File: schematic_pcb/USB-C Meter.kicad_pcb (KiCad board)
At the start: 2 copper layers, 58.5 x 48 mm, 11 parts, among them J1 USB_C_Receptacle_PowerOnly_6P, J2 USB_C_Receptacle_PowerOnly_6P, U1 WEMOS_D1_mini, U2 INA226, U3 Display I2C

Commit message: feat: pcb/schematic v2.1.0
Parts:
- removed R5: 3k3, Resistor_SMD:R_0402_1005Metric
- added C1: 33µF/35V, Capacitor_SMD:CP_Elec_5x5.8, F.Cu at (71.5, 33.0)
- added C10: 0.1µ, Capacitor_SMD:C_0603_1608Metric, B.Cu at (87.5, 53.5)
- added C11: 1µ, Capacitor_SMD:C_0603_1608Metric, B.Cu at (78.0, 51.5)
- added C12: 0.1µ, Capacitor_SMD:C_0603_1608Metric, B.Cu at (78.0, 50.0)
- added C14: 1µ, Capacitor_SMD:C_0603_1608Metric, B.Cu at (84.3, 42.0)
- added C15: 10n, Capacitor_SMD:C_0603_1608Metric, B.Cu at (85.8, 42.0)
- added C16: 0.1µ, Capacitor_SMD:C_0603_1608Metric, B.Cu at (89.5, 49.5)
- added C17: 1pF, Capacitor_SMD:C_0402_1005Metric, B.Cu at (88.0, 43.0)
- added C18: 1pF, Capacitor_SMD:C_0402_1005Metric, B.Cu at (88.0, 41.0)
- added C20: 0.1µ, Capacitor_SMD:C_0603_1608Metric, B.Cu at (85.8, 60.2)
- added C21: 0.1µ, Capacitor_SMD:C_0603_1608Metric, B.Cu at (82.8, 60.2)
- added C3: 10µF, Capacitor_SMD:C_0603_1608Metric, B.Cu at (73.1, 35.2)
- added C5: 10pF, Capacitor_SMD:C_0402_1005Metric, B.Cu at (81.8, 41.0)
- added C6: 220µF, Capacitor_SMD:CP_Elec_6.3x5.9, F.Cu at (94.0, 33.0)
- added C7: 220µF, Capacitor_SMD:CP_Elec_6.3x5.9, F.Cu at (82.5, 33.0)
- added C8: 0.1µ, Capacitor_SMD:C_0603_1608Metric, B.Cu at (77.0, 32.5)
- added C9: 10µF, Capacitor_SMD:C_0603_1608Metric, B.Cu at (78.5, 32.5)
- added D1: 1N5819WS, Diode_SMD:D_SOD-323, B.Cu at (67.0, 33.0)
- added D2: PMEG2005EH, Diode_SMD:D_SOD-123F, B.Cu at (100.0, 33.0)
- added D3: 1N5819WS, Diode_SMD:D_SOD-323, B.Cu at (70.0, 42.0)
- added D4: 1N5819WS, Diode_SMD:D_SOD-323, B.Cu at (96.5, 38.0)
- added J1: USB_B_Micro, Connector_USB:USB_Micro-B_Wuerth_629105150521, F.Cu at (62.4, 37.0)
- added J3: Generic IN, Connector_PinHeader_2.54mm:PinHeader_2x05_P2.54mm_Horizontal, F.Cu at (71.0, 56.2)
- added J4: Generic OUT, Connector_PinSocket_2.54mm:PinSocket_2x05_P2.54mm_Horizontal, F.Cu at (95.4, 56.3)
- added J6: Conn_Coaxial, Connector_Coaxial:U.FL_Hirose_U.FL-R-SMT-1_Vertical, F.Cu at (94.5, 41.0)
- added L1: 47µH, Inductor_SMD:L_Changjiang_FXL0630, F.Cu at (102.6, 36.8)
- added L2: 2.7nH, Inductor_SMD:L_0603_1608Metric_Pad1.05x0.95mm_HandSolder, B.Cu at (90.5, 42.0)
- added R10: 0.01R 3W, Resistor_SMD:R_2512_6332Metric, F.Cu at (83.5, 63.5)
- added R11: 10R, Resistor_SMD:R_0402_1005Metric, B.Cu at (85.5, 62.0)
- added R12: 12k, Resistor_SMD:R_0603_1608Metric_Pad0.98x0.95mm_HandSolder, B.Cu at (89.5, 51.0)
- added R2: 3k3, Resistor_SMD:R_0402_1005Metric, B.Cu at (87.5, 55.0)
- added R3: 400R, Resistor_SMD:R_0402_1005Metric, B.Cu at (84.0, 34.5)
- added R9: 10R, Resistor_SMD:R_0402_1005Metric, B.Cu at (83.0, 62.0)
- added REF**: MountingHole_2.2mm_M2_DIN965, MountingHole:MountingHole_2.2mm_M2_DIN965, F.Cu at (95.5, 62.2)
- added REF**: MountingHole_2.2mm_M2_DIN965, MountingHole:MountingHole_2.2mm_M2_DIN965, F.Cu at (62.0, 29.0)
- added REF**: MountingHole_2.2mm_M2_DIN965, MountingHole:MountingHole_2.2mm_M2_DIN965, F.Cu at (71.0, 62.2)
- added REF**: MountingHole_2.2mm_M2_DIN965, MountingHole:MountingHole_2.2mm_M2_DIN965, F.Cu at (104.5, 29.0)
- added U2: ME6211C33M5, Package_TO_SOT_SMD:SOT-23-5, B.Cu at (71.0, 32.5)
- added U3: TPS2115, Package_SO:TSSOP-8_4.4x3mm_P0.65mm, B.Cu at (84.0, 32.0)
- added U4: ESP32-C3FH4, Package_DFN_QFN:QFN-32-1EP_5x5mm_P0.5mm_EP3.7x3.7mm, B.Cu at (84.0, 48.0)
- added Y1: 40MHz, Crystal:Crystal_SMD_3225-4Pin_3.2x2.5mm, B.Cu at (79.0, 42.0)
- C13: renamed from C3; moved to B.Cu
- C2: value 20µ -> 10µF; footprint Capacitor_Tantalum_SMD:CP_EIA-6032-20_AVX-F -> Capacitor_SMD:C_0603_1608Metric; moved to B.Cu
- C4: value 0.1µ -> 10pF; footprint Capacitor_SMD:C_0603_1608Metric -> Capacitor_SMD:C_0402_1005Metric; moved to B.Cu
- J2: renamed from J1; value USB_C_Receptacle_PowerOnly_6P -> USB-C Receptacle 6P; footprint Connector_USB:USB_C_Receptacle_HRO_TYPE-C-31-M-17 -> Connector_USB:USB_C_Receptacle_GCT_USB4125-xx-x_6P_TopMnt_Horizontal
- J5: renamed from J2; value USB_C_Receptacle_PowerOnly_6P -> USB-C Receptacle 6P
- R1: value 0.01R 3W -> 3k3; footprint Resistor_SMD:R_1206_3216Metric -> Resistor_SMD:R_0402_1005Metric; moved to B.Cu
- R4: value 3k3 -> 12k; footprint Resistor_SMD:R_0402_1005Metric -> Resistor_SMD:R_0603_1608Metric_Pad0.98x0.95mm_HandSolder; moved to B.Cu
- U1: value WEMOS_D1_mini -> XL1509-3.3; footprint RF_Module:WEMOS_D1_mini_light -> Package_SO:SOIC-8_3.9x4.9mm_P1.27mm
- U6: renamed from U2; value INA226 -> INA228; moved to B.Cu
- U7: renamed from U3; footprint Connector_PinHeader_2.54mm:PinHeader_1x04_P2.54mm_Vertical -> Connector_PinSocket_2.54mm:PinSocket_1x04_P2.54mm_Vertical
- moved U1 27.6 mm to (94.0, 33.0), turned to 180 degrees
- moved C2 18.5 mm to (69.6, 35.2), turned to 180 degrees
- moved C4 14.4 mm to (81.8, 43.0), turned to 180 degrees
- moved J5 9.28 mm to (104.4, 64.0)
- moved R1 8.00 mm to (87.5, 56.5)
- moved C13 6.67 mm to (78.0, 48.5)
- moved U7 6.38 mm to (79.5, 38.5)
- moved U6 4.12 mm to (84.0, 56.0), turned to -90 degrees
- moved J2 3.54 mm to (62.0, 64.0)
- moved R4 2.50 mm to (89.5, 48.0), turned to 0 degrees
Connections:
- net Net-(J1-CC1) renamed /CC1
- net Net-(J1-CC2) renamed /CC2
- C13 pad 1: Net-(U1-3V3) -> GND
- C13 pad 2: Net-(J1-SHIELD) -> Net-(U4-VDD_SPI)
- C2 pad 1: Net-(U1-3V3) -> /VBUS_DATA_R
- C2 pad 2: Net-(J1-SHIELD) -> GND
- C4 pad 1: Net-(J1-SHIELD) -> Net-(U4-XTAL_N)
- C4 pad 2: Net-(U1-3V3) -> GND
- J2 pad A12: Net-(J1-SHIELD) -> GND
- J2 pad A9: Net-(U2-Vin+) -> /VBUS_PD_1_IN
- J2 pad B12: Net-(J1-SHIELD) -> GND
- J2 pad B9: Net-(U2-Vin+) -> /VBUS_PD_1_IN
- J2 pad S1: Net-(J1-SHIELD) -> GND
- J5 pad A12: Net-(J1-SHIELD) -> GND
- J5 pad A9: Net-(U2-Vbus) -> /VBUS_PD_2_IN
- J5 pad B12: Net-(J1-SHIELD) -> GND
- J5 pad B9: Net-(U2-Vbus) -> /VBUS_PD_2_IN
- J5 pad S1: Net-(J1-SHIELD) -> GND
- R1 pad 1: Net-(U2-Vin+) -> SDA
- R1 pad 2: Net-(U2-Vbus) -> 3V3
- R4 pad 1: Net-(U1-SCL/D1) -> Net-(U4-CHIP_EN)
- R4 pad 2: Net-(U1-3V3) -> 3V3
- U1 pad 1: unconnected-(U1-~{RST}-Pad1) -> /VBUS_PD_R
- U1 pad 2: unconnected-(U1-A0-Pad2) -> Net-(D2-K)
- U1 pad 3: unconnected-(U1-D0-Pad3) -> /VBUS_PD_3V3
- U1 pad 4: unconnected-(U1-SCK/D5-Pad4) -> GND
- U1 pad 5: unconnected-(U1-MISO/D6-Pad5) -> GND
- U1 pad 6: unconnected-(U1-MOSI/D7-Pad6) -> GND
- U1 pad 7: unconnected-(U1-CS/D8-Pad7) -> GND
- U1 pad 8: Net-(U1-3V3) -> GND
- U6 pad 1: Net-(J1-SHIELD) -> GND
- U6 pad 10: Net-(U2-Vin+) -> /SHNT+
- U6 pad 2: Net-(U1-3V3) -> 3V3
- U6 pad 4: Net-(U1-SDA/D2) -> SDA
- U6 pad 5: Net-(U1-SCL/D1) -> SCL
- U6 pad 6: Net-(U1-3V3) -> 3V3
- U6 pad 7: Net-(J1-SHIELD) -> GND
- U6 pad 8: Net-(U2-Vbus) -> /SHNT-
- U6 pad 9: Net-(U2-Vbus) -> /SHNT-
- U7 pad 1: Net-(U1-3V3) -> 3V3
- U7 pad 2: Net-(J1-SHIELD) -> GND
- U7 pad 3: Net-(U1-SCL/D1) -> SDA
- U7 pad 4: Net-(U1-SDA/D2) -> SCL
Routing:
- net GND: track 0.00 -> 221.5 mm, vias 0 -> 11
- net /VBUS_PD_1_IN: track 0.00 -> 111.7 mm, vias 0 -> 8
- net 3V3: track 0.00 -> 84.6 mm, vias 0 -> 6
- net Net-(J1-SHIELD): track 70.5 -> 0.00 mm, vias 2 -> 0
- net /VBUS_PD_2_IN: track 0.00 -> 70.4 mm, vias 0 -> 7
- net Net-(U1-3V3): track 57.0 -> 0.00 mm
- net Net-(U2-Vbus): track 41.1 -> 0.00 mm
- net /VBUS_PD_R: track 0.00 -> 39.0 mm, vias 0 -> 1
- net Net-(U2-Vin+): track 36.9 -> 0.00 mm
- net /CHGR_ID_GENERIC: track 0.00 -> 32.0 mm
- net /VBUS_PD_3V3: track 0.00 -> 29.2 mm, vias 0 -> 2
- net SDA: track 0.00 -> 28.6 mm, vias 0 -> 2
- net Net-(U1-SCL/D1): track 27.5 -> 0.00 mm
- net Net-(U1-SDA/D2): track 27.1 -> 0.00 mm
- net Net-(J1-D+): track 0.00 -> 23.0 mm, vias 0 -> 1
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- added copper zone on B.Cu, net /VBUS_PD_1_IN
- added copper zone on F.Cu, net /VBUS_PD_1_IN
- added copper zone on B.Cu, net /VBUS_PD_2_IN
- added copper zone on F.Cu, net /VBUS_PD_2_IN
- added copper zone on B.Cu, net GND
- added copper zone on F.Cu, net GND
- removed copper zone on B.Cu, net Net-(J1-SHIELD)
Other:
- board size 58.5 x 48 mm -> 49.4 x 45 mm
- board text added: "MacWake USB-C Meter V2.0"
- board text added: "PWR_IN"
- board text added: "PWR_OUT"
- board text removed: "MacWake USB-C Meter V1.1"

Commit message: feat: pcb/schematic v2.1.1
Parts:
- removed the REF** at (95.5, 62.2)
- removed the REF** at (62.0, 29.0)
- removed the REF** at (71.0, 62.2)
- removed the REF** at (104.5, 29.0)
- added J7: UART, Connector_PinHeader_1.00mm:PinHeader_1x04_P1.00mm_Vertical_SMD_Pin1Left, F.Cu at (75.6, 46.0)
- added R13: 12k, Resistor_SMD:R_0603_1608Metric_Pad0.98x0.95mm_HandSolder, B.Cu at (78.0, 55.5)
- added R14: 12k, Resistor_SMD:R_0603_1608Metric_Pad0.98x0.95mm_HandSolder, B.Cu at (78.0, 54.0)
- added REF**: MountingHole_2.2mm_M2_DIN965_Pad, MountingHole:MountingHole_2.2mm_M2_DIN965_Pad, F.Cu at (95.5, 64.2)
- added REF**: MountingHole_2.2mm_M2_DIN965_Pad, MountingHole:MountingHole_2.2mm_M2_DIN965_Pad, F.Cu at (63.0, 29.2)
- added REF**: MountingHole_2.2mm_M2_DIN965_Pad, MountingHole:MountingHole_2.2mm_M2_DIN965_Pad, F.Cu at (103.0, 29.2)
- added REF**: MountingHole_2.2mm_M2_DIN965_Pad, MountingHole:MountingHole_2.2mm_M2_DIN965_Pad, F.Cu at (71.0, 64.2)
- added TP1: Boot, TestPoint:TestPoint_Pad_D1.5mm, B.Cu at (79.5, 58.5)
- added TP2: Expansion, TestPoint:TestPoint_Pad_D1.5mm, B.Cu at (76.5, 58.5)
- added TP3: RST, TestPoint:TestPoint_Pad_D1.5mm, B.Cu at (91.0, 45.5)
- C2, C3: value 10µF -> 10µF/10V
- C21: value 0.1µ -> 0.1µF/6.3V
- C4, C5: value 10pF -> 27pF
- D1, D3, D4: footprint Diode_SMD:D_SOD-323 -> Diode_SMD:D_SOD-123F
- R1, R2: footprint Resistor_SMD:R_0402_1005Metric -> Resistor_SMD:R_0603_1608Metric_Pad0.98x0.95mm_HandSolder
- U2: value ME6211C33M5 -> ME6211C33
- moved C10 2.24 mm to (89.5, 52.5)
- moved R1 2.24 mm to (89.5, 55.5)
- moved R2 2.24 mm to (89.5, 54.0)
- moved C2 1.61 mm to (71.0, 36.0), turned to -90 degrees
- moved C11 1.00 mm to (78.0, 52.5)
- moved C12 1.00 mm to (78.0, 51.0)
- moved C13 1.00 mm to (78.0, 49.5)
- moved D1 1.00 mm to (68.0, 33.0)
- moved U2 1.00 mm to (72.0, 32.5)
- moved C3 0.84 mm to (73.1, 36.0), turned to -90 degrees
- moved C14 0.66 mm to (85.0, 42.0)
- moved C15 0.66 mm to (86.5, 42.0)
- moved Y1 0.65 mm to (79.7, 42.0)
- moved C1 0.50 mm to (71.5, 32.5)
- moved C6 0.50 mm to (94.0, 32.5)
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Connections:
- U4 pad 15: unconnected-(U4-GPIO9-Pad15) -> Net-(U4-GPIO9)
- U4 pad 16: unconnected-(U4-GPIO10-Pad16) -> Net-(U4-GPIO10)
- U4 pad 27: unconnected-(U4-U0RXD-Pad27) -> Net-(J7-Pin_2)
- U4 pad 28: unconnected-(U4-U0TXD-Pad28) -> Net-(J7-Pin_3)
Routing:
- net GND: track 221.5 -> 197.8 mm
- net Net-(J7-Pin_3): track 0.00 -> 11.1 mm, vias 0 -> 1
- net Net-(U4-GPIO10): track 0.00 -> 10.2 mm
- net Net-(U4-GPIO9): track 0.00 -> 9.38 mm
- net Net-(J7-Pin_2): track 0.00 -> 8.46 mm, vias 0 -> 1
- net Net-(U4-CHIP_EN): track 3.39 -> 9.13 mm, vias 0 -> 2
- net /VBUS_PD_3V3: track 29.2 -> 34.2 mm
- net /VBUS_DATA_3V3: track 12.7 -> 11.2 mm
- net Net-(U4-XTAL_P): track 8.29 -> 6.95 mm
- net Net-(U4-XTAL_N): track 9.18 -> 8.05 mm
- net /CC2: track 39.9 -> 41.0 mm
- net /VBUS_PD_R: track 39.0 -> 38.0 mm
- net /SHNT-: track 4.88 -> 5.86 mm
- net SDA: track 28.6 -> 29.5 mm
- net SCL: track 22.2 -> 22.9 mm
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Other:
- board text added: "MacWake USB-C Meter V2.2"

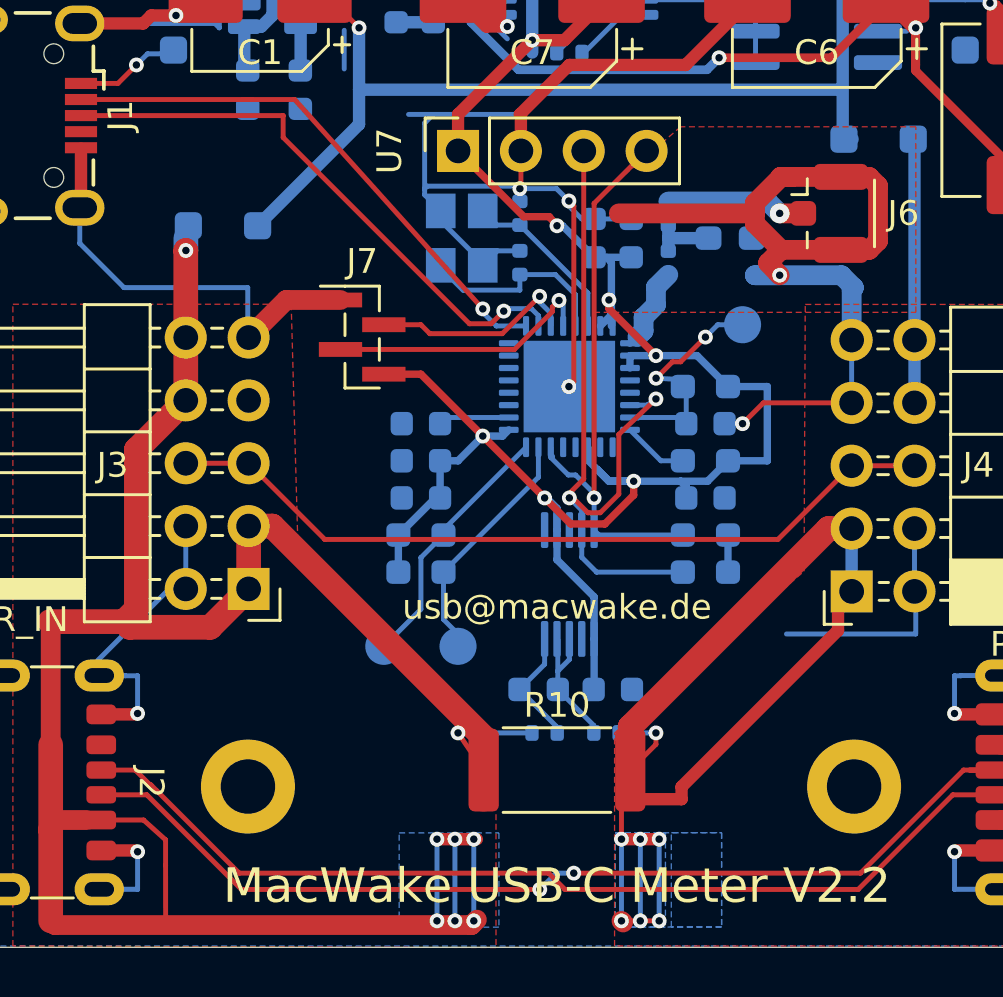
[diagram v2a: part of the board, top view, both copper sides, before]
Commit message: fix(pcb): fixed sda/scl pin mismatch at display connector
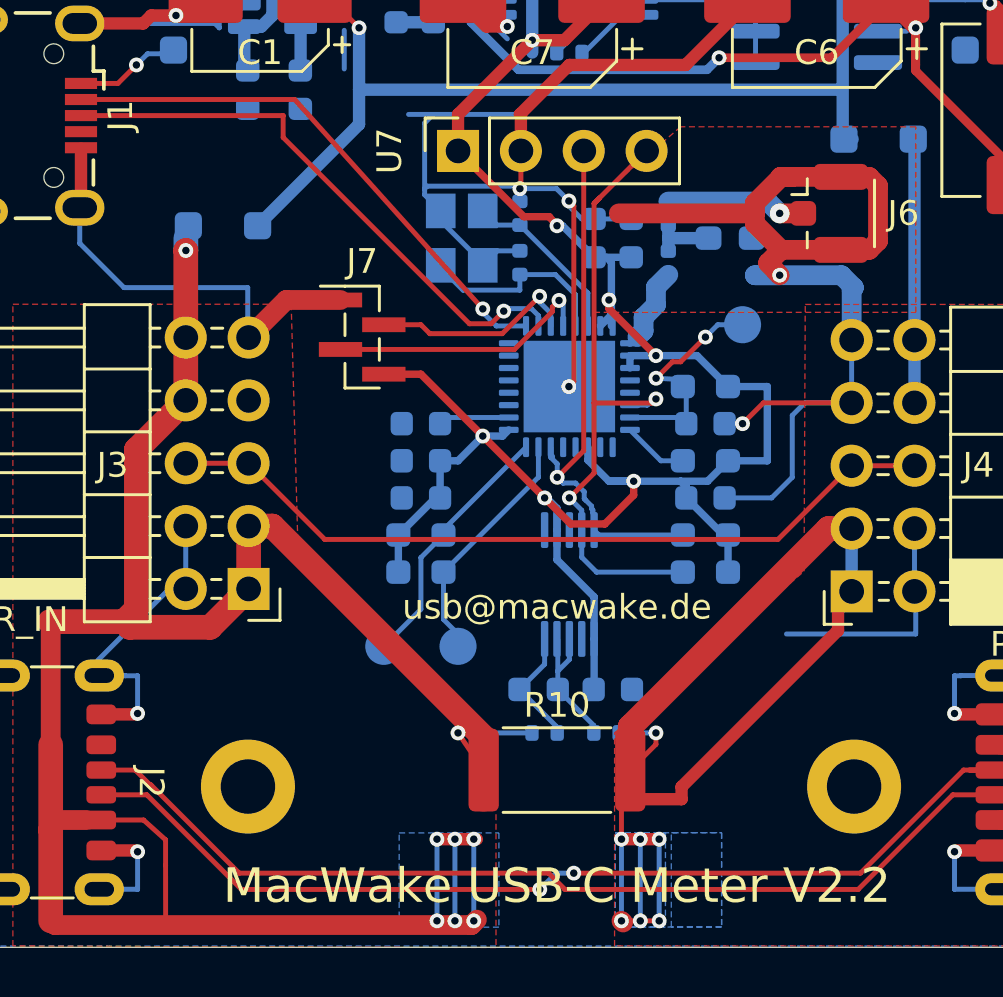
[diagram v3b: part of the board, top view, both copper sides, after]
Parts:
- TP3: value RST -> Reset
- renumbered REF** to MH1, REF** to MH2, REF** to MH3, REF** to MH4
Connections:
- U7 pad 3: SDA -> SCL
- U7 pad 4: SCL -> SDA
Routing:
- net GND: track 197.8 -> 206.0 mm
- net SDA: track 29.5 -> 26.5 mm
- net 3V3: track 85.1 -> 86.6 mm
- net SCL: track 22.9 -> 21.8 mm
